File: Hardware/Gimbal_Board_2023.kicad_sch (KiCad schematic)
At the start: 72 parts, among them J1 6P6C, J2 RJ45_LED_Shielded, Q1 Q_NMOS_GDS, Q2 Q_NMOS_GDS, Q3 Q_NMOS_GDS, Q4 Q_NMOS_GDS, Q5 Q_NMOS_GDS, Q6 Q_NMOS_GDS, Q7 Q_NMOS_GDS, SW1 SW_Push, SW2 SW_Push, SW3 SW_Push, SW4 SW_Push, SW5 SW_Push, SW6 SW_Push, SW7 SW_Push, SW9 SW_DPDT_x2, U1 OKI, U3 Teensy4.1_DEV-16771, U5 TSR_1-2450

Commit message: organized schematic and changed yellow to blue and blue to yellow for LED
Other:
- moved on the sheet: C1, C2, C3, Conn1A, Conn1D, Conn6, Conn7, Conn8, D1, D2, D3, D4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

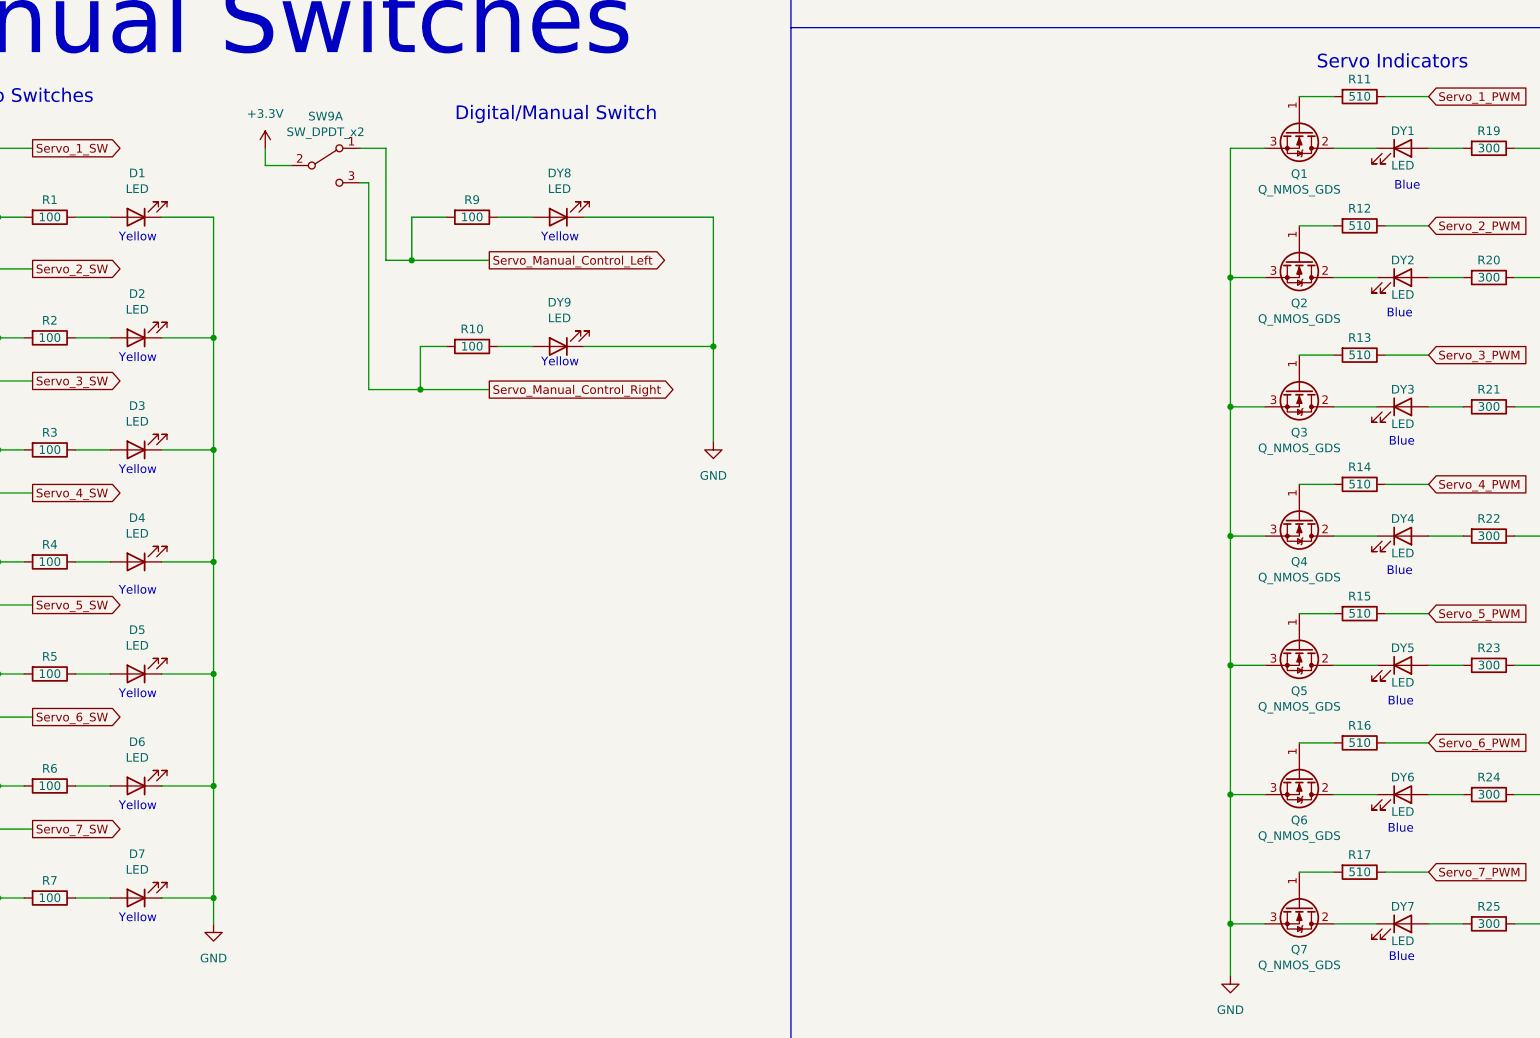
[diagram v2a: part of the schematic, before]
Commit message: Reassigned labels
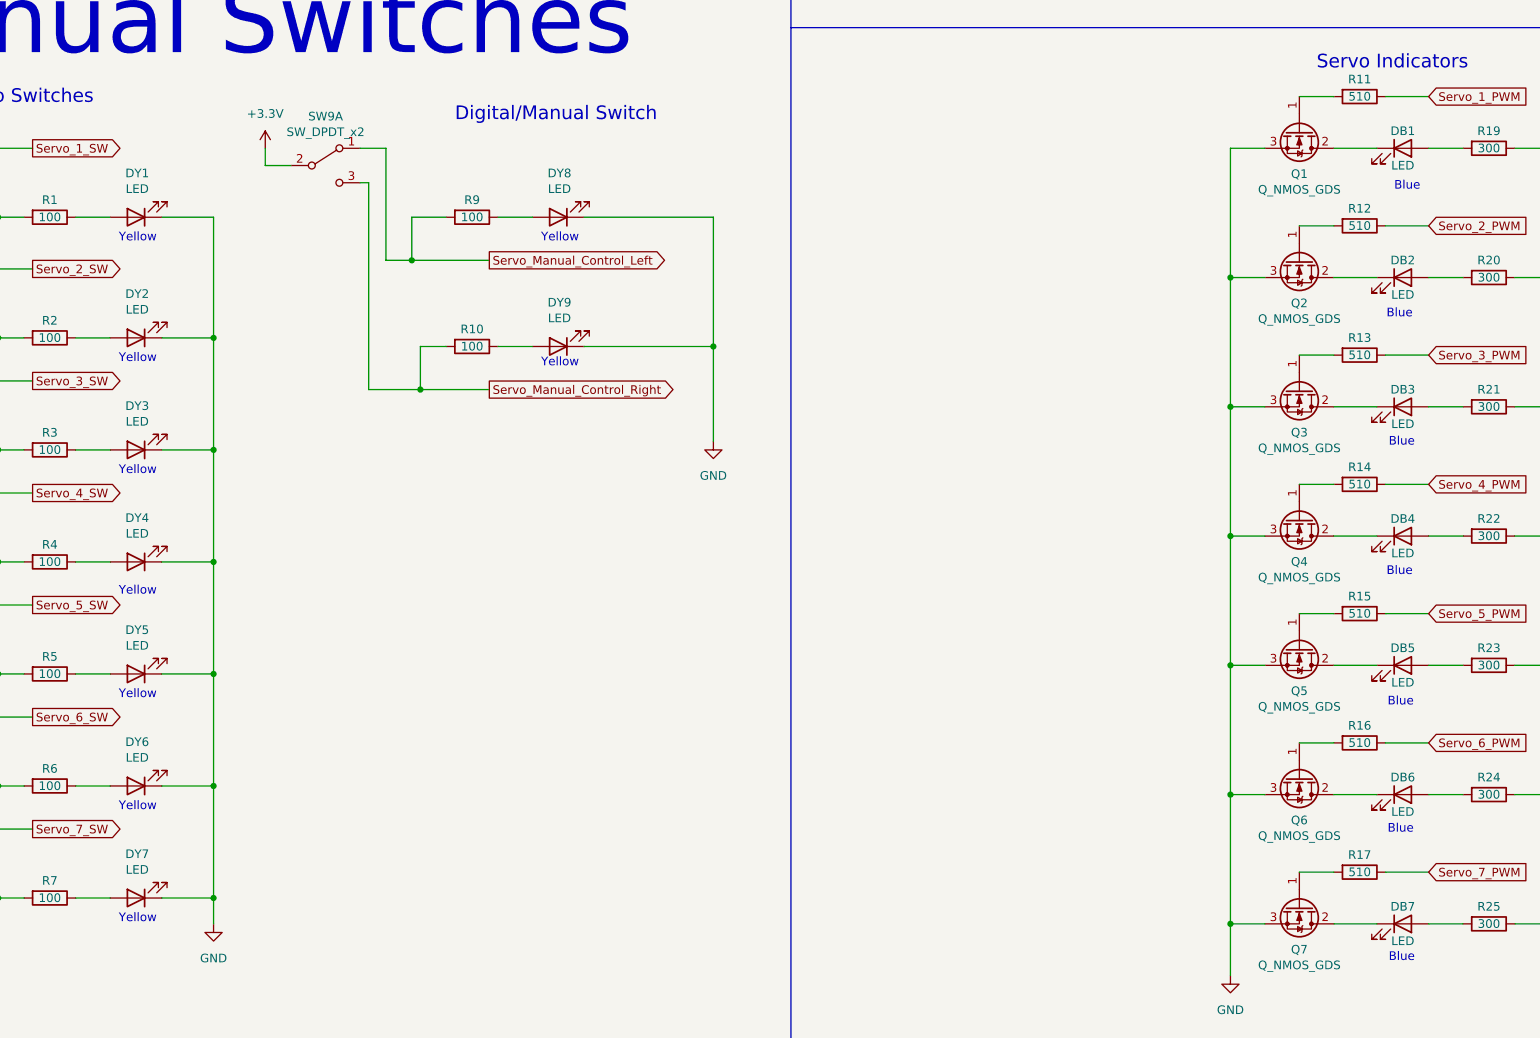
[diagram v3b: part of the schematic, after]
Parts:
- renumbered DY1 to DB1, DY2 to DB2, DY3 to DB3, DY4 to DB4, DY5 to DB5, DY6 to DB6, DY7 to DB7, D1 to DY1, D2 to DY2, D3 to DY3, D4 to DY4, D5 to DY5, D6 to DY6, D7 to DY7
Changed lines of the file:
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@@
   (symbol (lib_id "Device:LED") (at 62.23 162.56 180) (unit 1)
     (in_bom yes) (on_board yes)
-    (property "Reference" "D1" (id 0) (at 62.4078 156.083 0))
+    (property "Reference" "DY1" (id 0) (at 62.4078 156.083 0))
     (property "Value" "LED" (id 1) (at 62.4078 158.3944 0))
     (property "Footprint" "LED_SMD:LED_0603_1608Metric_Pad1.05x0.95mm_HandSolder" (id 2) (at 62.23 162.56 0)
@@
   (symbol (lib_id "Device:LED") (at 248.92 266.7 0) (unit 1)
     (in_bom yes) (on_board yes)
-    (property "Reference" "DY7" (id 0) (at 248.92 264.16 0))
+    (property "Reference" "DB7" (id 0) (at 248.92 264.16 0))
     (property "Value" "LED" (id 1) (at 248.92 269.24 0))
     (property "Footprint" "LED_SMD:LED_0603_1608Metric_Pad1.05x0.95mm_HandSolder" (id 2) (at 248.92 266.7 0)
@@
   (symbol (lib_id "Device:LED") (at 248.92 228.6 0) (unit 1)
     (in_bom yes) (on_board yes)
-    (property "Reference" "DY5" (id 0) (at 248.92 226.06 0))
+    (property "Reference" "DB5" (id 0) (at 248.92 226.06 0))
     (property "Value" "LED" (id 1) (at 248.92 231.14 0))
     (property "Footprint" "LED_SMD:LED_0603_1608Metric_Pad1.05x0.95mm_HandSolder" (id 2) (at 248.92 228.6 0)
@@
   (symbol (lib_id "Device:LED") (at 248.92 247.65 0) (unit 1)
     (in_bom yes) (on_board yes)
-    (property "Reference" "DY6" (id 0) (at 248.92 245.11 0))
+    (property "Reference" "DB6" (id 0) (at 248.92 245.11 0))
     (property "Value" "LED" (id 1) (at 248.92 250.19 0))
     (property "Footprint" "LED_SMD:LED_0603_1608Metric_Pad1.05x0.95mm_HandSolder" (id 2) (at 248.92 247.65 0)
@@
   (symbol (lib_id "Device:LED") (at 248.92 152.4 0) (unit 1)
     (in_bom yes) (on_board yes)
-    (property "Reference" "DY1" (id 0) (at 248.92 149.86 0))
+    (property "Reference" "DB1" (id 0) (at 248.92 149.86 0))
     (property "Value" "LED" (id 1) (at 248.92 154.94 0))
     (property "Footprint" "LED_SMD:LED_0603_1608Metric_Pad1.05x0.95mm_HandSolder" (id 2) (at 248.92 152.4 0)
@@
   (symbol (lib_id "Device:LED") (at 62.23 262.89 180) (unit 1)
     (in_bom yes) (on_board yes)
-    (property "Reference" "D7" (id 0) (at 62.4078 256.413 0))
+    (property "Reference" "DY7" (id 0) (at 62.4078 256.413 0))
     (property "Value" "LED" (id 1) (at 62.4078 258.7244 0))
     (property "Footprint" "LED_SMD:LED_0603_1608Metric_Pad1.05x0.95mm_HandSolder" (id 2) (at 62.23 262.89 0)
@@
   (symbol (lib_id "Device:LED") (at 62.23 246.38 180) (unit 1)
     (in_bom yes) (on_board yes)
-    (property "Reference" "D6" (id 0) (at 62.4078 239.903 0))
+    (property "Reference" "DY6" (id 0) (at 62.4078 239.903 0))
     (property "Value" "LED" (id 1) (at 62.4078 242.2144 0))
     (property "Footprint" "LED_SMD:LED_0603_1608Metric_Pad1.05x0.95mm_HandSolder" (id 2) (at 62.23 246.38 0)
@@
   (symbol (lib_id "Device:LED") (at 248.92 209.55 0) (unit 1)
     (in_bom yes) (on_board yes)
-    (property "Reference" "DY4" (id 0) (at 248.92 207.01 0))
+    (property "Reference" "DB4" (id 0) (at 248.92 207.01 0))
     (property "Value" "LED" (id 1) (at 248.92 212.09 0))
     (property "Footprint" "LED_SMD:LED_0603_1608Metric_Pad1.05x0.95mm_HandSolder" (id 2) (at 248.92 209.55 0)
@@
   (symbol (lib_id "Device:LED") (at 248.92 190.5 0) (unit 1)
     (in_bom yes) (on_board yes)
-    (property "Reference" "DY3" (id 0) (at 248.92 187.96 0))
+    (property "Reference" "DB3" (id 0) (at 248.92 187.96 0))
     (property "Value" "LED" (id 1) (at 248.92 193.04 0))
     (property "Footprint" "LED_SMD:LED_0603_1608Metric_Pad1.05x0.95mm_HandSolder" (id 2) (at 248.92 190.5 0)
@@
   (symbol (lib_id "Device:LED") (at 62.23 180.34 180) (unit 1)
     (in_bom yes) (on_board yes)
-    (property "Reference" "D2" (id 0) (at 62.4078 173.863 0))
+    (property "Reference" "DY2" (id 0) (at 62.4078 173.863 0))
     (property "Value" "LED" (id 1) (at 62.4078 176.1744 0))
     (property "Footprint" "LED_SMD:LED_0603_1608Metric_Pad1.05x0.95mm_HandSolder" (id 2) (at 62.23 180.34 0)
@@
   (symbol (lib_id "Device:LED") (at 62.23 213.36 180) (unit 1)
     (in_bom yes) (on_board yes)
-    (property "Reference" "D4" (id 0) (at 62.4078 206.883 0))
+    (property "Reference" "DY4" (id 0) (at 62.4078 206.883 0))
     (property "Value" "LED" (id 1) (at 62.4078 209.1944 0))
     (property "Footprint" "LED_SMD:LED_0603_1608Metric_Pad1.05x0.95mm_HandSolder" (id 2) (at 62.23 213.36 0)
@@
   (symbol (lib_id "Device:LED") (at 62.23 229.87 180) (unit 1)
     (in_bom yes) (on_board yes)
-    (property "Reference" "D5" (id 0) (at 62.4078 223.393 0))
+    (property "Reference" "DY5" (id 0) (at 62.4078 223.393 0))
     (property "Value" "LED" (id 1) (at 62.4078 225.7044 0))
     (property "Footprint" "LED_SMD:LED_0603_1608Metric_Pad1.05x0.95mm_HandSolder" (id 2) (at 62.23 229.87 0)
@@
   (symbol (lib_id "Device:LED") (at 248.92 171.45 0) (unit 1)
     (in_bom yes) (on_board yes)
-    (property "Reference" "DY2" (id 0) (at 248.92 168.91 0))
+    (property "Reference" "DB2" (id 0) (at 248.92 168.91 0))
     (property "Value" "LED" (id 1) (at 248.92 173.99 0))
     (property "Footprint" "LED_SMD:LED_0603_1608Metric_Pad1.05x0.95mm_HandSolder" (id 2) (at 248.92 171.45 0)
@@
   (symbol (lib_id "Device:LED") (at 62.23 196.85 180) (unit 1)
     (in_bom yes) (on_board yes)
-    (property "Reference" "D3" (id 0) (at 62.4078 190.373 0))
+    (property "Reference" "DY3" (id 0) (at 62.4078 190.373 0))
     (property "Value" "LED" (id 1) (at 62.4078 192.6844 0))
     (property "Footprint" "LED_SMD:LED_0603_1608Metric_Pad1.05x0.95mm_HandSolder" (id 2) (at 62.23 196.85 0)
@@
       (reference "Conn8") (unit 1) (value "Molex_SL_03") (footprint "")
     )
-    (path "/0b1b924b-b37f-4488-a7c0-24b98962bc4f"
-      (reference "D1") (unit 1) (value "LED") (footprint "LED_SMD:LED_0603_1608Metric_Pad1.05x0.95mm_HandSolder")
-    )
-    (path "/a3f90619-84a9-44fa-a87c-765196542cb1"
-      (reference "D2") (unit 1) (value "LED") (footprint "LED_SMD:LED_0603_1608Metric_Pad1.05x0.95mm_HandSolder")
-    )
-    (path "/f870acaf-b5ce-4d73-9d5c-be47631144d9"
-      (reference "D3") (unit 1) (value "LED") (footprint "LED_SMD:LED_0603_1608Metric_Pad1.05x0.95mm_HandSolder")
-    )
-    (path "/a600d5d5-eb24-407e-9e89-52c1af1c9bd3"
-      (reference "D4") (unit 1) (value "LED") (footprint "LED_SMD:LED_0603_1608Metric_Pad1.05x0.95mm_HandSolder")
-    )
-    (path "/c1c71399-c8af-45b7-907a-3606e540d9e8"
-      (reference "D5") (unit 1) (value "LED") (footprint "LED_SMD:LED_0603_1608Metric_Pad1.05x0.95mm_HandSolder")
-    )
-    (path "/640ea6c0-80c0-49f6-95b7-bd5c28c9c34a"
-      (reference "D6") (unit 1) (value "LED") (footprint "LED_SMD:LED_0603_1608Metric_Pad1.05x0.95mm_HandSolder")
-    )
-    (path "/381caaa7-17c5-40d1-bb74-e4acec601354"
-      (reference "D7") (unit 1) (value "LED") (footprint "LED_SMD:LED_0603_1608Metric_Pad1.05x0.95mm_HandSolder")
+    (path "/2efdf2af-1cd9-4ea1-8da8-577ea0c613f7"
+      (reference "DB1") (unit 1) (value "LED") (footprint "LED_SMD:LED_0603_1608Metric_Pad1.05x0.95mm_HandSolder")
+    )
+    (path "/d486f80b-80a6-4efb-8fb4-d1503c5f3a41"
+      (reference "DB2") (unit 1) (value "LED") (footprint "LED_SMD:LED_0603_1608Metric_Pad1.05x0.95mm_HandSolder")
+    )
+    (path "/7e8d689e-1920-45f1-8937-33da51e53ee0"
+      (reference "DB3") (unit 1) (value "LED") (footprint "LED_SMD:LED_0603_1608Metric_Pad1.05x0.95mm_HandSolder")
+    )
+    (path "/6e4de53b-fd35-4dd3-ba33-679a6ffc63a8"
+      (reference "DB4") (unit 1) (value "LED") (footprint "LED_SMD:LED_0603_1608Metric_Pad1.05x0.95mm_HandSolder")
+    )
+    (path "/1f9db72c-71e6-47e1-91c6-a16be9479425"
+      (reference "DB5") (unit 1) (value "LED") (footprint "LED_SMD:LED_0603_1608Metric_Pad1.05x0.95mm_HandSolder")
+    )
+    (path "/2e1dabfb-874a-413f-aa00-7e9516846447"
+      (reference "DB6") (unit 1) (value "LED") (footprint "LED_SMD:LED_0603_1608Metric_Pad1.05x0.95mm_HandSolder")
+    )
+    (path "/172d2e58-8338-4841-83c8-fc304bfb14b5"
+      (reference "DB7") (unit 1) (value "LED") (footprint "LED_SMD:LED_0603_1608Metric_Pad1.05x0.95mm_HandSolder")
     )
     (path "/fc2c166c-658d-426b-bff9-27e0dfedefb2"
@@
       (reference "DG2") (unit 1) (value "LED") (footprint "")
     )
-    (path "/2efdf2af-1cd9-4ea1-8da8-577ea0c613f7"
+    (path "/0b1b924b-b37f-4488-a7c0-24b98962bc4f"
       (reference "DY1") (unit 1) (value "LED") (footprint "LED_SMD:LED_0603_1608Metric_Pad1.05x0.95mm_HandSolder")
     )
-    (path "/d486f80b-80a6-4efb-8fb4-d1503c5f3a41"
+    (path "/a3f90619-84a9-44fa-a87c-765196542cb1"
       (reference "DY2") (unit 1) (value "LED") (footprint "LED_SMD:LED_0603_1608Metric_Pad1.05x0.95mm_HandSolder")
     )
-    (path "/7e8d689e-1920-45f1-8937-33da51e53ee0"
+    (path "/f870acaf-b5ce-4d73-9d5c-be47631144d9"
       (reference "DY3") (unit 1) (value "LED") (footprint "LED_SMD:LED_0603_1608Metric_Pad1.05x0.95mm_HandSolder")
     )
-    (path "/6e4de53b-fd35-4dd3-ba33-679a6ffc63a8"
+    (path "/a600d5d5-eb24-407e-9e89-52c1af1c9bd3"
       (reference "DY4") (unit 1) (value "LED") (footprint "LED_SMD:LED_0603_1608Metric_Pad1.05x0.95mm_HandSolder")
     )
-    (path "/1f9db72c-71e6-47e1-91c6-a16be9479425"
+    (path "/c1c71399-c8af-45b7-907a-3606e540d9e8"
       (reference "DY5") (unit 1) (value "LED") (footprint "LED_SMD:LED_0603_1608Metric_Pad1.05x0.95mm_HandSolder")
     )
-    (path "/2e1dabfb-874a-413f-aa00-7e9516846447"
+    (path "/640ea6c0-80c0-49f6-95b7-bd5c28c9c34a"
       (reference "DY6") (unit 1) (value "LED") (footprint "LED_SMD:LED_0603_1608Metric_Pad1.05x0.95mm_HandSolder")
     )
-    (path "/172d2e58-8338-4841-83c8-fc304bfb14b5"
+    (path "/381caaa7-17c5-40d1-bb74-e4acec601354"
       (reference "DY7") (unit 1) (value "LED") (footprint "LED_SMD:LED_0603_1608Metric_Pad1.05x0.95mm_HandSolder")
     )
